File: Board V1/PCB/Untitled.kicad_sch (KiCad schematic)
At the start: 10 parts, among them U1 MCP2515-xSO, U2 LM78L05_SO8, Y1 16MHz

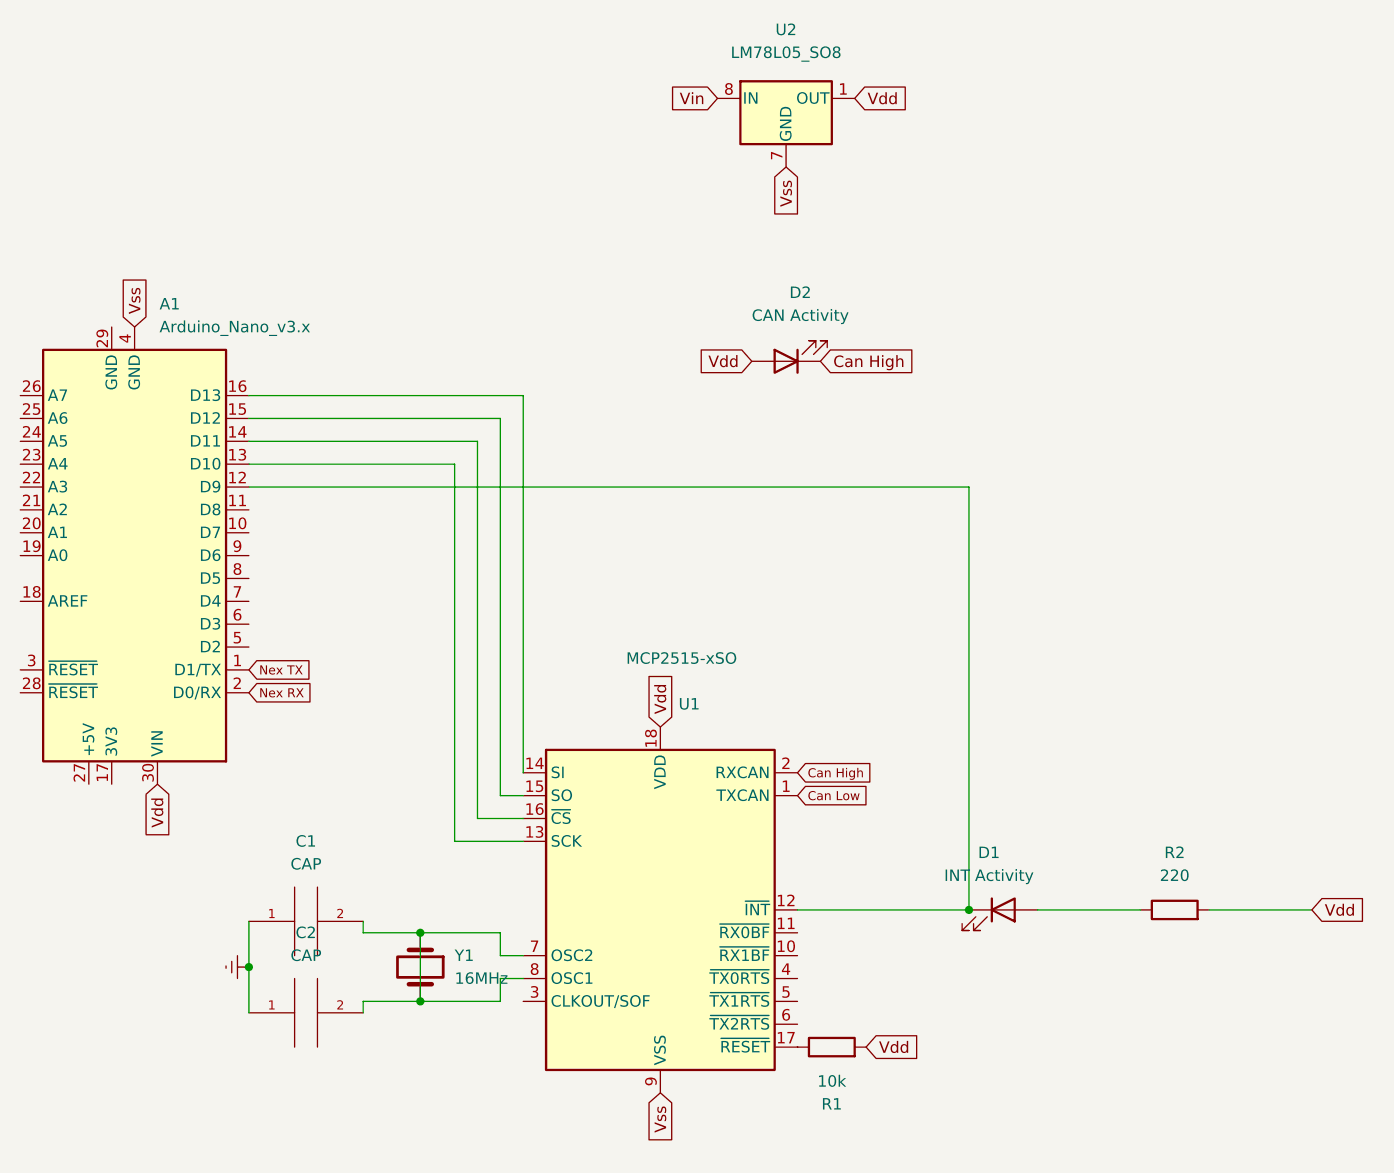
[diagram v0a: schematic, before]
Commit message: Added new version of board with correct can chips
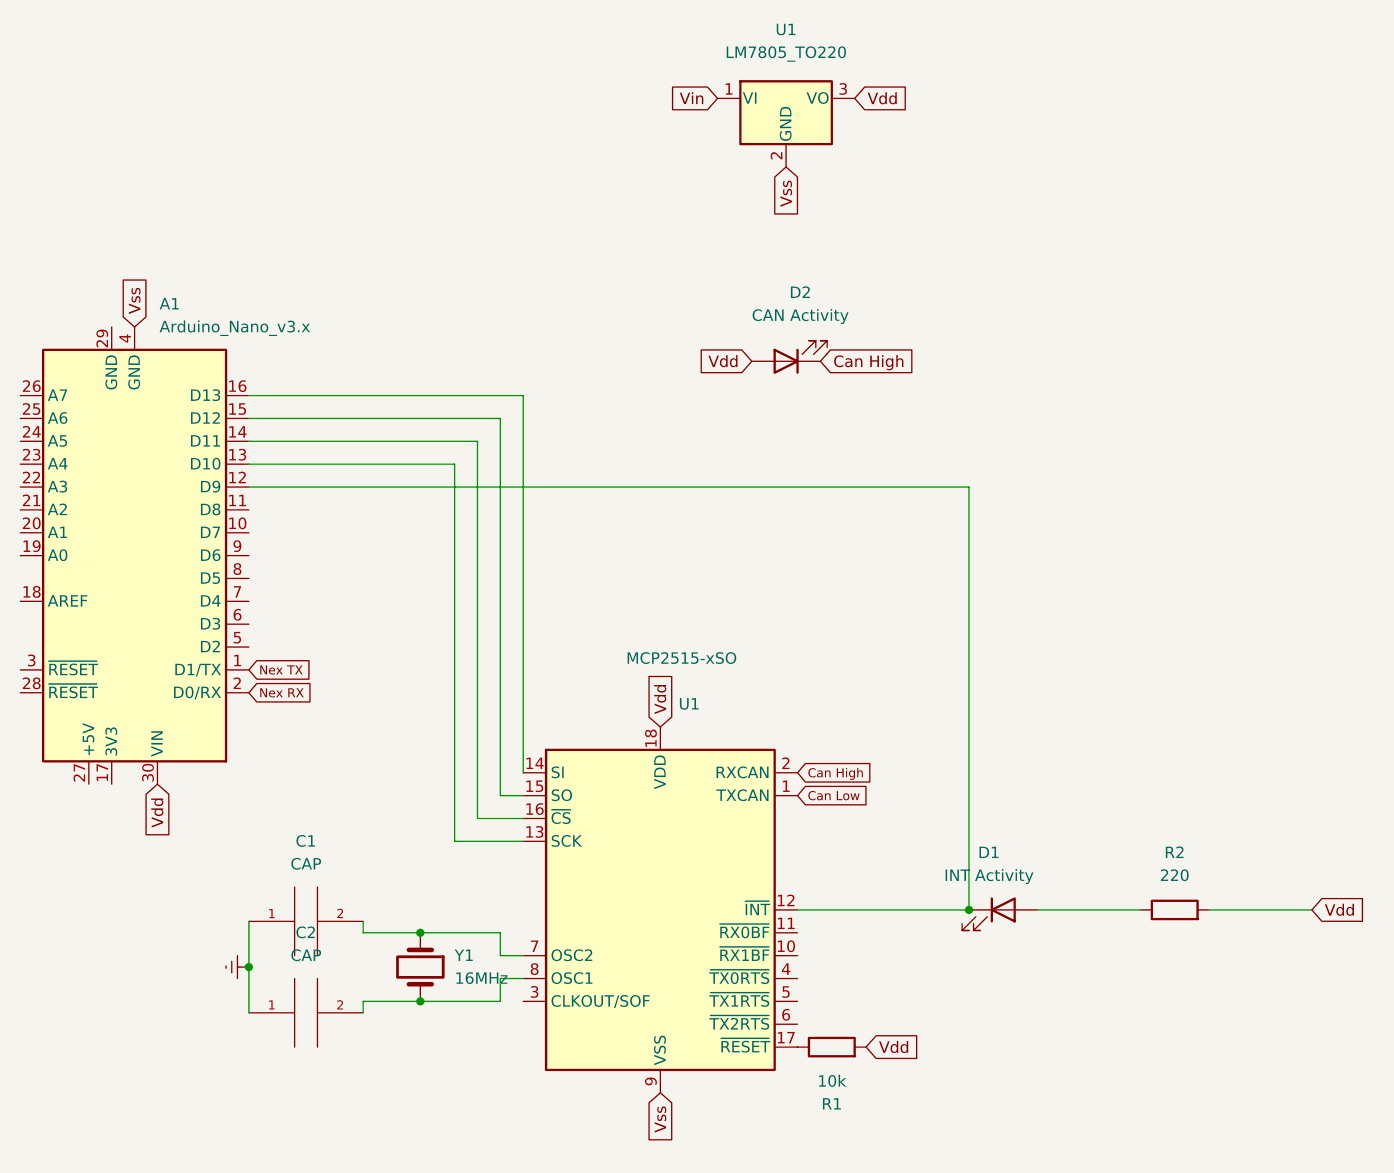
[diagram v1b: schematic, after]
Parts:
- removed U2: LM78L05_SO8, Package_SO:SOIC-8_3.9x4.9mm_P1.27mm, symbol Regulator_Linear:LM78L05_SO8
- added U1: LM7805_TO220, Package_TO_SOT_THT:TO-220-3_Vertical, symbol Regulator_Linear:LM7805_TO220
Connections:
- net Vdd: now also U1.3 (VO)
- net Vin: now also U1.1 (VI)
- net Vss: now also U1.2 (GND)
- net at C1.2, U1.7 (OSC2), Y1.1: no longer C2.2, U1.8 (OSC1), Y1.2
- new net: C2.2, U1.8 (OSC1), Y1.2
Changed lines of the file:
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@@
-    (stroke (width 0) (type default) (color 0 0 0 0))
-  )
-  (wire (pts (xy 135.89 129.54) (xy 135.89 137.16))
     (stroke (width 0) (type default) (color 0 0 0 0))
   )
@@
     (pin "2")
   )
-  (symbol (lib_id "Regulator_Linear:LM78L05_SO8") (at 176.53 36.83 0) (unit 1)
-    (in_bom yes) (on_board yes) (fields_autoplaced)
-    (property "Reference" "U2" (id 0) (at 176.53 29.21 0))
-    (property "Value" "LM78L05_SO8" (id 1) (at 176.53 31.75 0))
-    (property "Footprint" "Package_SO:SOIC-8_3.9x4.9mm_P1.27mm" (id 2) (at 179.07 31.75 0)
-      (effects (font (size 1.27 1.27) italic) hide)
-    )
-    (property "Datasheet" "https://www.onsemi.com/pub/Collateral/MC78L06A-D.pdf" (id 3) (at 181.61 36.83 0)
-      (effects (font (size 1.27 1.27)) hide)
-    )
-    (pin "1")
-    (pin "2")
-    (pin "3")
-    (pin "4")
-    (pin "5")
-    (pin "6")
-    (pin "7")
-    (pin "8")
-  )
   (symbol (lib_id "pspice:CAP") (at 123.19 128.27 90) (unit 1)
     (in_bom yes) (on_board yes) (fields_autoplaced)
@@
     (pin "1")
     (pin "2")
+  )
+  (symbol (lib_id "Regulator_Linear:LM7805_TO220") (at 176.53 36.83 0) (unit 1)
+    (in_bom yes) (on_board yes) (fields_autoplaced)
+    (property "Reference" "U1" (id 0) (at 176.53 29.21 0))
+    (property "Value" "LM7805_TO220" (id 1) (at 176.53 31.75 0))
+    (property "Footprint" "Package_TO_SOT_THT:TO-220-3_Vertical" (id 2) (at 176.53 31.115 0)
+      (effects (font (size 1.27 1.27) italic) hide)
+    )
+    (property "Datasheet" "https://www.onsemi.cn/PowerSolutions/document/MC7800-D.PDF" (id 3) (at 176.53 38.1 0)
+      (effects (font (size 1.27 1.27)) hide)
+    )
+    (pin "1")
+    (pin "2")
+    (pin "3")
   )
   (symbol (lib_id "Device:R") (at 181.61 142.24 90) (unit 1)
@@
       (reference "U1") (unit 1) (value "MCP2515-xSO") (footprint "Package_SO:SOIC-18W_7.5x11.6mm_P1.27mm")
     )
-    (path "/3d0d4fe2-d788-494f-ae99-68086ae96c0e"
-      (reference "U2") (unit 1) (value "LM78L05_SO8") (footprint "Package_SO:SOIC-8_3.9x4.9mm_P1.27mm")
+    (path "/9f7ea62b-a73e-4a7c-8a42-a6eac497ba26"
+      (reference "U1") (unit 1) (value "LM7805_TO220") (footprint "Package_TO_SOT_THT:TO-220-3_Vertical")
     )
     (path "/9ccba75c-11b7-4564-adb5-241a14fdc74f"
